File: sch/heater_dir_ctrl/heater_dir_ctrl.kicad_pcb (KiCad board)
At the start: 2 copper layers, 75 parts, among them J1 UV light, J10 main, J11 flashlight, J2 SWD, J3 heater, J4 heater, J5 motor, J6 motor, J7 ac_in, J8 ac_in, J9 ., Q1 MMBTA42, Q2 MMBTA42, Q3 MMBTA42, Q4 MMBTA42, Q5 AO3400, Q6 Q_Photo_NPN_CE, Q7 AO3400, SW1 SW_Push, SW2 SW_Push, U1 XC6206-33, U2 STM32F031F4Px, U4 4069, U5 TM1637, U7 LTV-817, U8 LNK306D

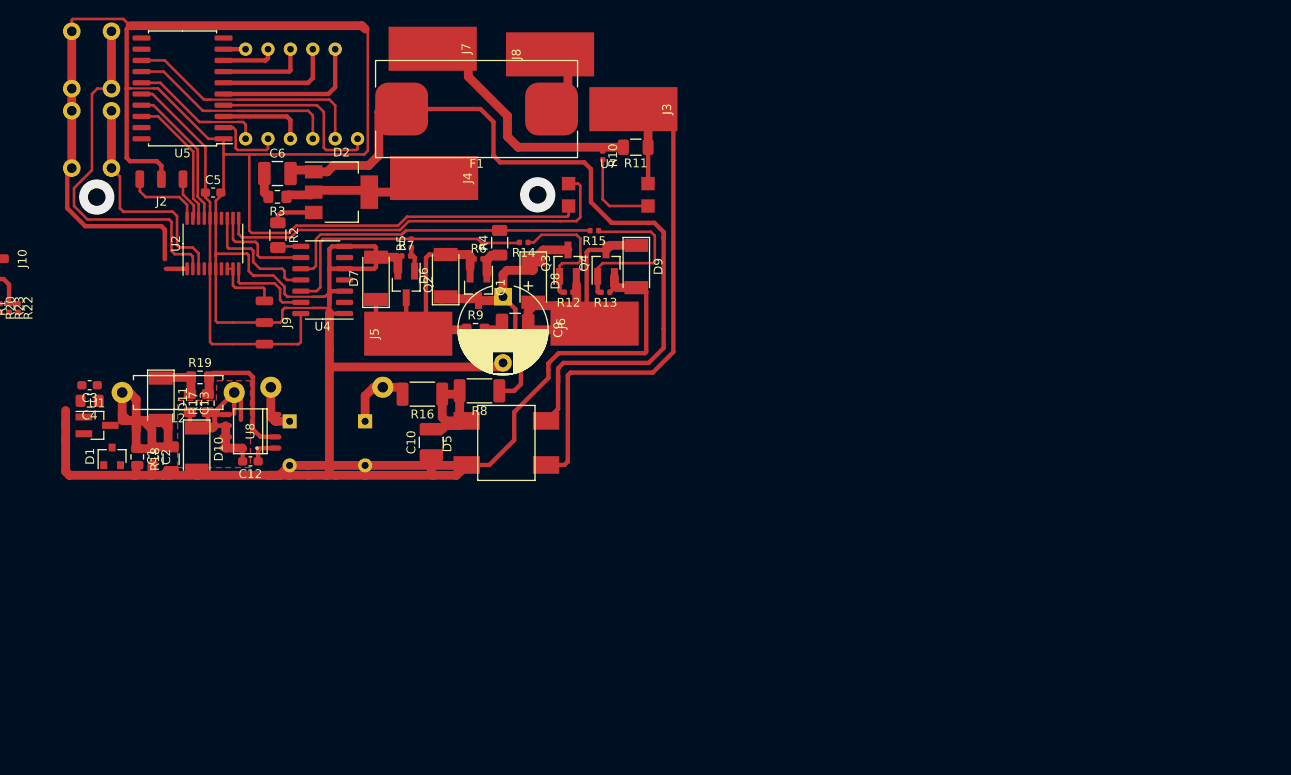
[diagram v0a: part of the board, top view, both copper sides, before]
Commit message: sch w new transistors
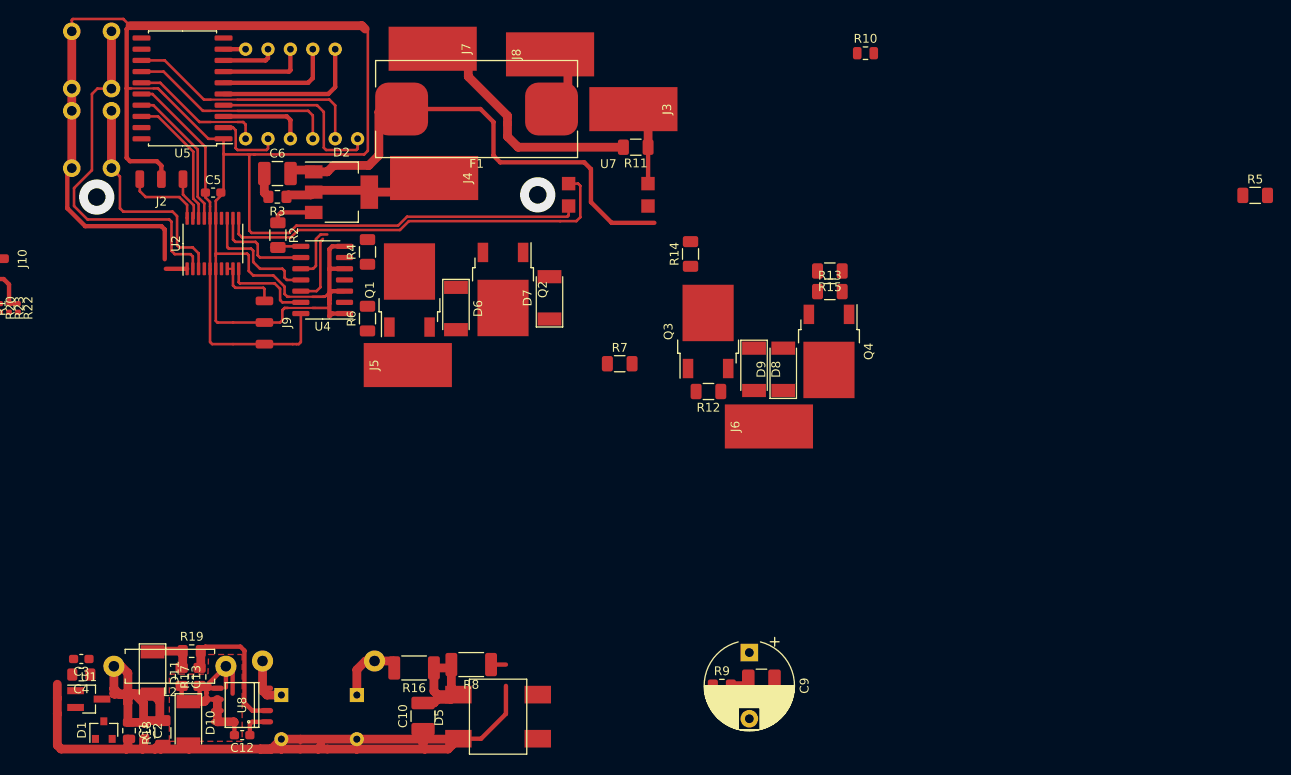
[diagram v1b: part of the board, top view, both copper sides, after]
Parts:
- Q1, Q2, Q3, Q4: value MMBTA42 -> 2N60; footprint Package_TO_SOT_SMD:SOT-23_Handsoldering -> Package_TO_SOT_SMD:TO-252-2
- R10: footprint Resistor_SMD:R_0402_1005Metric -> Resistor_SMD:R_0805_2012Metric
- R12, R13, R14, R15, R5, R6, R7: footprint Resistor_SMD:R_0402_1005Metric -> Resistor_SMD:R_1206_3216Metric
- U2: value STM32F031F4Px -> STM32F031F4P6
- moved R5 95.8 mm to (177.6, 107.0), turned to 0 degrees
- moved C8 49.1 mm to (121.6, 162.1)
- moved C9 49.1 mm to (120.3, 158.8)
- moved R9 49.1 mm to (117.1, 162.6)
- moved R10 32.0 mm to (133.4, 90.9), turned to 0 degrees
- moved C1 31.1 mm to (49.9, 167.7)
- moved C10 31.1 mm to (83.3, 166.0)
- moved C12 31.1 mm to (62.8, 168.2)
- moved C2 31.1 mm to (51.8, 167.7)
- moved C3 31.1 mm to (44.5, 159.6)
- moved C4 31.1 mm to (44.5, 161.3)
- moved L1 31.1 mm to (77.8, 159.8)
- moved R16 31.1 mm to (82.2, 160.6)
- moved R8 31.1 mm to (88.7, 160.2)
- moved U8 31.1 mm to (62.7, 164.8)
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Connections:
- Q1 pad 2: Net-(D6-Pad2) -> Net-(C9-Pad1)
- Q1 pad 3: Net-(C9-Pad1) -> Net-(D6-Pad2)
- Q2 pad 2: GND -> Net-(D6-Pad2)
- Q2 pad 3: Net-(D6-Pad2) -> GND
- Q3 pad 2: Net-(C8-Pad1) -> Net-(C9-Pad1)
- Q3 pad 3: Net-(C9-Pad1) -> Net-(C8-Pad1)
- Q4 pad 2: GND -> Net-(C8-Pad1)
- Q4 pad 3: Net-(C8-Pad1) -> GND
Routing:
- net GND: track 453.4 -> 362.9 mm
- net Net-(D6-Pad2): track 54.7 -> 0.00 mm
- net LINE: track 73.2 -> 21.2 mm
- net Net-(C8-Pad1): track 51.6 -> 0.00 mm
- net NEUT: track 97.4 -> 62.7 mm
- net Net-(C9-Pad1): track 35.2 -> 3.16 mm
- net Net-(R15-Pad2): track 36.6 -> 6.40 mm
- net Net-(R14-Pad2): track 30.6 -> 8.01 mm
- net Net-(Q4-Pad1): track 19.4 -> 0.00 mm
- net Net-(Q3-Pad1): track 15.0 -> 0.00 mm
- net Net-(R10-Pad2): track 9.94 -> 0.00 mm
- net Net-(Q2-Pad1): track 3.38 -> 0.00 mm
- net Net-(Q1-Pad1): track 3.28 -> 0.00 mm

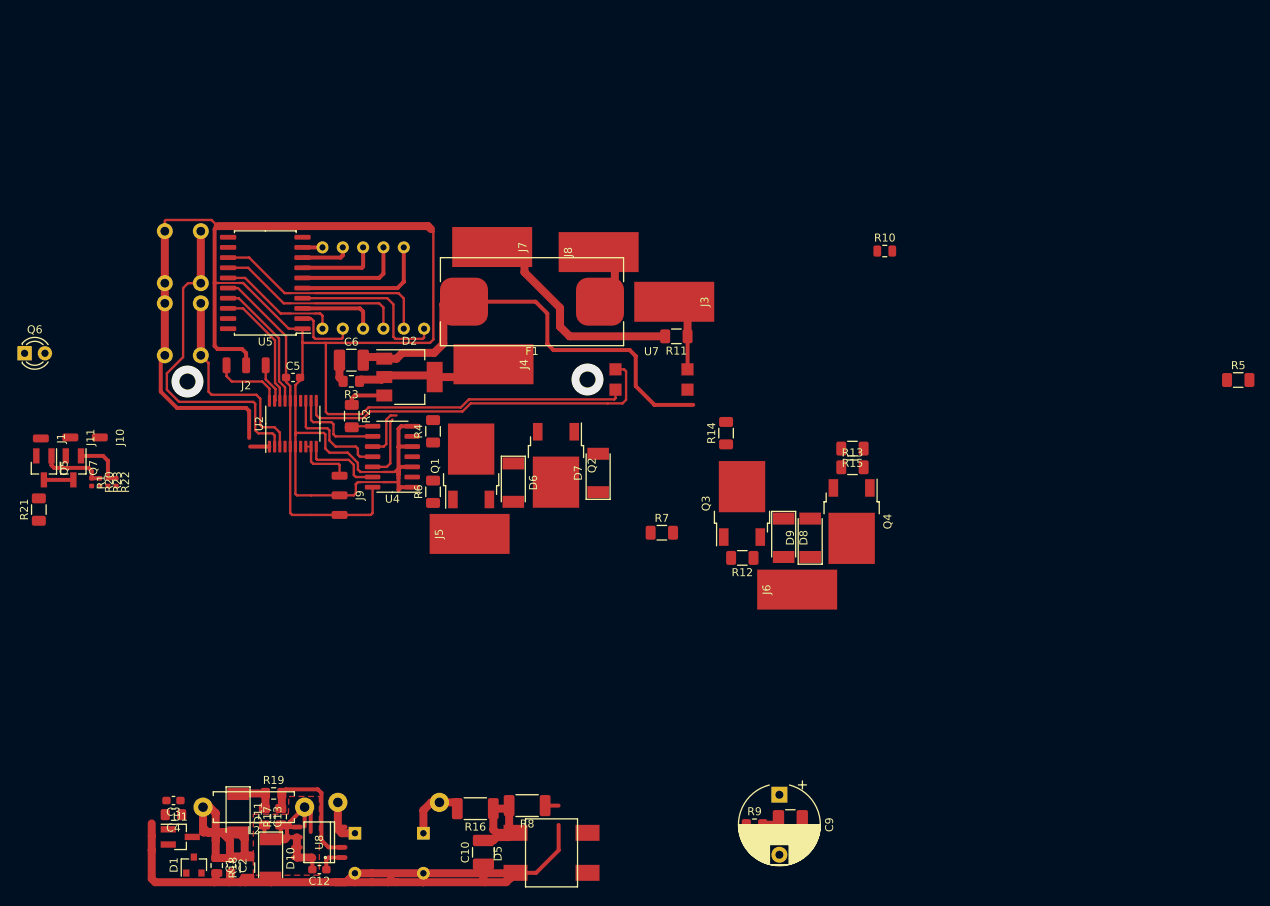
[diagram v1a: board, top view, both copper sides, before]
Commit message: PCB with new transistors
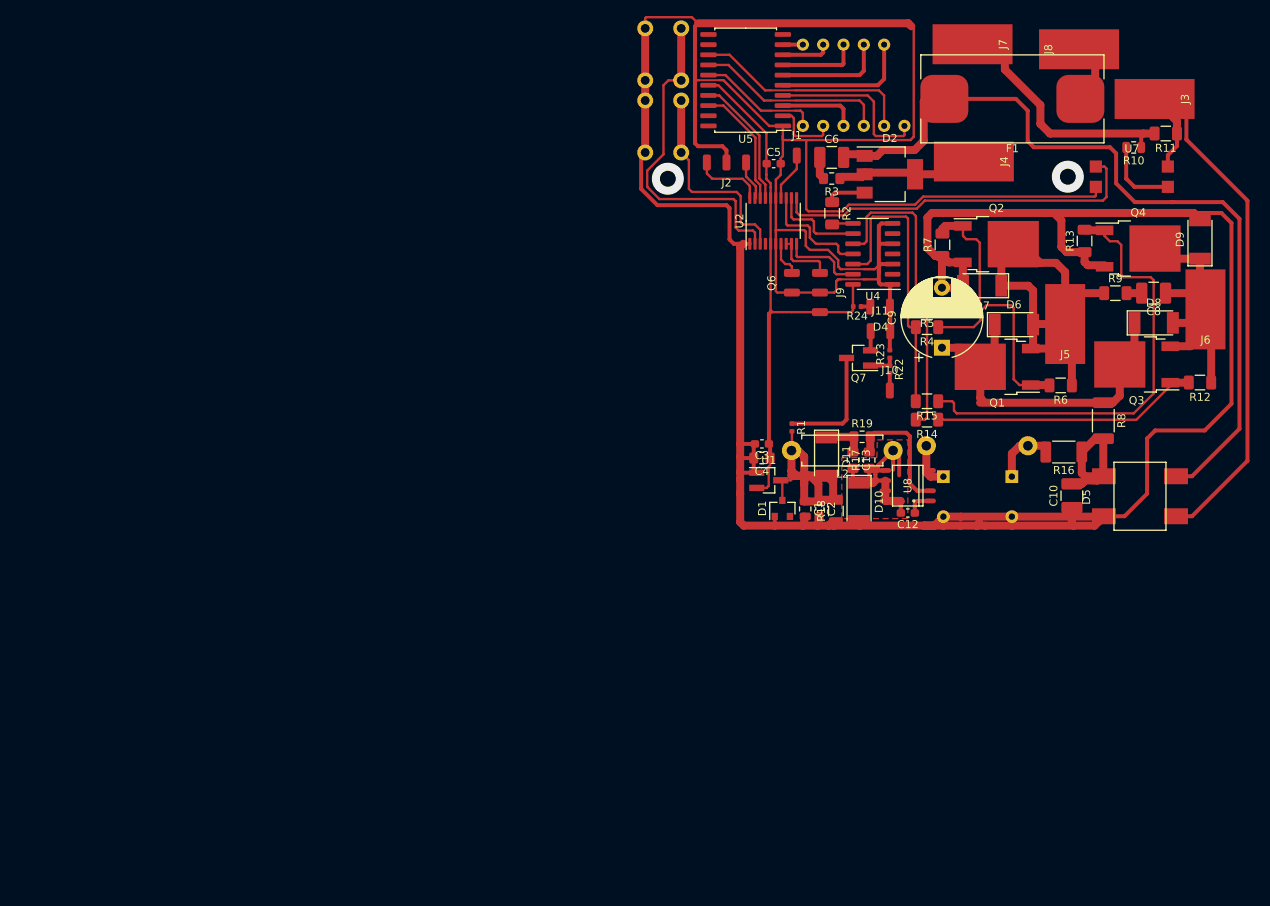
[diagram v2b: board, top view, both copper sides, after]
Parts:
- removed Q5: AO3400, Package_TO_SOT_SMD:SOT-23_Handsoldering
- removed R20: 50, Resistor_SMD:R_0402_1005Metric
- removed R21: 390, Resistor_SMD:R_1206_3216Metric
- added D4: IR204A, local:2WIRE_PADS, F.Cu at (132.9, 97.8)
- added R24: 1k, Resistor_SMD:R_0402_1005Metric, F.Cu at (130.0, 97.8)
- J1: value UV light -> JMP1
- J10: value main -> JMP1
- J11: value flashlight -> UV; footprint Connector_Wire:SolderWirePad_1x01_SMD_1x2mm -> local:2WIRE_PADS
- Q6: footprint LED_THT:LED_D3.0mm -> local:2WIRE_PADS
- R1: value 50 -> 220
- R9: footprint Resistor_SMD:R_0805_2012Metric_Pad1.15x1.40mm_HandSolder -> Resistor_SMD:R_1206_3216Metric
- moved J11 102.1 mm to (132.8, 100.9), turned to 0 degrees
- moved J1 100.9 mm to (122.4, 78.9), turned to 0 degrees
- moved Q7 99.1 mm to (130.1, 104.2), turned to 180 degrees
- moved R23 99.0 mm to (134.1, 103.7), turned to 90 degrees
- moved J10 98.9 mm to (134.1, 108.3), turned to 0 degrees
- moved R22 97.7 mm to (134.1, 105.7)
- moved Q6 96.3 mm to (121.8, 94.9), turned to 90 degrees
- moved R1 87.8 mm to (121.8, 112.9)
- moved R8 86.6 mm to (160.7, 112.1), turned to 270 degrees
- moved C1 86.0 mm to (123.5, 123.1)
- moved C10 86.0 mm to (156.8, 121.5)
- moved C12 86.0 mm to (136.3, 123.6)
- moved C13 86.0 mm to (129.5, 117.0)
- moved C2 86.0 mm to (125.3, 123.1)
- moved C3 86.0 mm to (118.1, 115.0)
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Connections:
- C1 pad 2: Net-(C1-Pad2) -> GND
- C11 pad 2: Net-(C1-Pad2) -> GND
- C2 pad 2: Net-(C1-Pad2) -> GND
- C3 pad 2: Net-(C1-Pad2) -> GND
- C4 pad 2: Net-(C1-Pad2) -> GND
- C7 pad 2: Net-(C1-Pad2) -> GND
- D1 pad 2: Net-(C1-Pad2) -> GND
- D10 pad 2: Net-(C1-Pad2) -> GND
- D5 pad 2: Net-(C1-Pad2) -> GND
- J10 pad 1: GND -> Net-(J10-Pad1)
- Q6 pad 1: Net-(Q6-Pad1) -> GND
- Q6 pad 2: GND -> Net-(Q6-Pad2)
- Q7 pad 3: Net-(Q5-Pad3) -> Net-(Q7-Pad3)
- R1 pad 1: Net-(Q5-Pad1) -> Net-(Q7-Pad3)
- R1 pad 2: Net-(R1-Pad2) -> +5V
- R18 pad 1: Net-(C1-Pad2) -> GND
- R22 pad 2: Net-(R22-Pad2) -> Net-(J10-Pad1)
- U1 pad 1: Net-(C1-Pad2) -> GND
- U2 pad 14: Net-(R1-Pad2) -> Net-(J1-Pad1)
- U2 pad 6: Net-(U2-Pad6) -> GND
- U2 pad 7: Net-(Q6-Pad1) -> Net-(Q6-Pad2)
- U4 pad 1: Net-(R1-Pad2) -> GND
- U4 pad 10: Net-(R15-Pad2) -> Net-(R14-Pad2)
- U4 pad 12: Net-(R14-Pad2) -> Net-(R15-Pad2)
- U4 pad 2: Net-(R22-Pad2) -> Net-(U4-Pad2)
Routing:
- net GND: track 362.9 -> 522.1 mm
- net LINE: track 21.2 -> 87.9 mm
- net Net-(D6-Pad2): track 0.00 -> 60.3 mm
- net Net-(Q4-Pad1): track 0.00 -> 57.4 mm
- net Net-(C8-Pad1): track 0.00 -> 46.7 mm
- net NEUT: track 62.7 -> 108.7 mm
- net Net-(C9-Pad1): track 3.16 -> 44.1 mm
- net Net-(Q3-Pad1): track 0.00 -> 33.5 mm
- net Net-(R14-Pad2): track 8.01 -> 39.4 mm
- net Net-(R15-Pad2): track 6.40 -> 36.2 mm
- net Net-(Q1-Pad1): track 0.00 -> 25.1 mm
- net +3V3: track 46.0 -> 69.7 mm
- net Net-(Q2-Pad1): track 0.00 -> 19.9 mm
- net Net-(Q7-Pad3): track 0.00 -> 14.7 mm
- net Net-(R10-Pad2): track 0.00 -> 9.53 mm
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
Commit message: didn't fit
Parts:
- moved R15 2.17 mm to (136.8, 108.7)
- moved R24 2.16 mm to (127.8, 97.8)
- moved R14 2.16 mm to (136.7, 111.1)
- moved J11 2.03 mm to (130.8, 100.9)
- moved Q7 2.03 mm to (128.1, 104.2)
- moved R22 1.98 mm to (132.1, 105.7)
- moved R23 1.98 mm to (132.1, 103.7)
- moved C8 1.98 mm to (165.1, 96.1)
- moved C9 1.98 mm to (138.6, 103.0)
- moved D4 1.98 mm to (130.9, 97.8)
- moved D6 1.98 mm to (147.6, 100.1)
- moved D7 1.98 mm to (143.6, 95.2)
- moved D8 1.98 mm to (165.1, 99.9)
- moved D9 1.98 mm to (170.8, 89.4)
- moved J10 1.98 mm to (132.1, 108.3)
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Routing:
- net GND: track 522.1 -> 545.3 mm
- net NEUT: track 108.7 -> 118.1 mm
- net +5V: track 41.4 -> 50.3 mm
- net LINE: track 87.9 -> 80.2 mm
- net Net-(SW1-Pad2): track 41.7 -> 38.2 mm
- net VPP: track 18.3 -> 21.5 mm
- net Net-(SW2-Pad2): track 26.2 -> 23.1 mm
- net Net-(U2-Pad11): track 46.6 -> 49.3 mm
- net Net-(J7-Pad1): track 33.4 -> 36.0 mm
- net Net-(Q3-Pad1): track 33.5 -> 35.7 mm
- net Net-(Q7-Pad3): track 14.7 -> 12.7 mm
- net Net-(J1-Pad1): track 6.12 -> 8.09 mm
- net Net-(Q4-Pad1): track 57.4 -> 59.3 mm
- net Net-(D2-Pad3): track 5.03 -> 6.59 mm
- net +3V3: track 69.7 -> 70.9 mm
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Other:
- net class Default: clearance 0.2 -> 0.5
- rule trace_clearance: 0.2 -> 0.5

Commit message: drivers
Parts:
- removed the C8 at (165.1, 96.1)
- removed the C9 at (138.6, 103.0)
- removed the D1 at (120.6, 123.1)
- removed D4: IR204A, local:2WIRE_PADS
- removed the D7 at (143.6, 95.2)
- removed the J10 at (132.1, 108.3)
- removed the J11 at (130.8, 100.9)
- removed the Q3 at (162.9, 105.1)
- removed the R4 at (136.7, 100.4)
- removed the R5 at (136.7, 98.1)
- removed the R6 at (153.4, 107.7)
- removed the R7 at (138.7, 90.1)
- removed the U1 at (118.9, 119.5)
- removed the U4 at (130.3, 91.2)
- added C11: 10uF, Capacitor_SMD:C_0805_2012Metric, F.Cu at (193.0, 94.7)
- added C12: 22uF 400V, Capacitor_THT:CP_Radial_D10.0mm_P7.50mm, F.Cu at (285.9, 51.2)
- added C13: 100n, Capacitor_SMD:C_1210_3225Metric_Pad1.33x2.70mm_HandSolder, F.Cu at (216.7, 94.9)
- added C14: 10uF, Capacitor_SMD:C_0805_2012Metric, F.Cu at (227.9, 100.1)
- added D10: 1N4007, Diode_SMD:D_MELF, F.Cu at (215.4, 100.8)
- added D11: 1N4007, Diode_SMD:D_MELF, F.Cu at (221.1, 84.4)
- added D13: MBR0530, Diode_SMD:D_SOD-123, F.Cu at (232.9, 103.5)
- added D5: MBR0530, Diode_SMD:D_SOD-123, F.Cu at (189.1, 91.3)
- added J2: JMP1, Connector_Wire:SolderWirePad_1x01_SMD_1x2mm, F.Cu at (80.9, 102.7)
- added J3: UV, local:2WIRE_PADS, F.Cu at (79.9, 97.9)
- added Q5: 2N60, Package_TO_SOT_SMD:TO-252-2, F.Cu at (202.1, 100.1)
- added Q6: 2N60, Package_TO_SOT_SMD:TO-252-2, F.Cu at (220.6, 102.2)
- added Q8: DTD114E, Package_TO_SOT_SMD:SOT-23_Handsoldering, F.Cu at (126.9, 86.4)
- added Q9: DTD114E, Package_TO_SOT_SMD:SOT-23_Handsoldering, F.Cu at (233.9, 93.9)
- added R16: 100k, Resistor_SMD:R_0402_1005Metric, F.Cu at (122.4, 83.6)
- added R17: 220, Resistor_SMD:R_1206_3216Metric, F.Cu at (221.5, 95.4)
- added R18: 220, Resistor_SMD:R_1206_3216Metric, F.Cu at (225.7, 88.6)
- added R19: 100k, Resistor_SMD:R_0402_1005Metric, F.Cu at (123.4, 83.6)
- added R20: 220, Resistor_SMD:R_1206_3216Metric, F.Cu at (225.3, 98.6)
- added R21: 220, Resistor_SMD:R_1206_3216Metric, F.Cu at (226.8, 92.0)
- added R25: 100k, Resistor_SMD:R_0402_1005Metric, F.Cu at (231.6, 95.6)
- added R26: 1, Resistor_SMD:R_2010_5025Metric, F.Cu at (191.4, 84.5)
- added R27: 1, Resistor_SMD:R_2010_5025Metric, F.Cu at (215.4, 109.2)
- added R28: 220, Resistor_SMD:R_1206_3216Metric, F.Cu at (182.7, 91.3)
- added R29: 220, Resistor_SMD:R_1206_3216Metric, F.Cu at (182.9, 102.4)
- added U3: AP1117-33, Package_TO_SOT_SMD:SOT-223-3_TabPin2, F.Cu at (117.4, 141.7)
- added U5: IRS2103, Package_SO:SSOP-8_3.9x5.05mm_P1.27mm, F.Cu at (188.2, 95.4)
- added U8: IRS2103, Package_SO:SSOP-8_3.9x5.05mm_P1.27mm, F.Cu at (232.8, 99.4)
- D6: value 1N4007 -> IR204A; footprint Diode_SMD:D_MELF -> local:2WIRE_PADS
- Q1: value 2N60 -> AO3400; footprint Package_TO_SOT_SMD:TO-252-2 -> Package_TO_SOT_SMD:SOT-23_Handsoldering
- Q2: value 2N60 -> DTD114E; footprint Package_TO_SOT_SMD:TO-252-2 -> Package_TO_SOT_SMD:SOT-23_Handsoldering
- Q7: value AO3400 -> 2N60; footprint Package_TO_SOT_SMD:SOT-23_Handsoldering -> Package_TO_SOT_SMD:TO-252-2
- R10: value 1к -> 100; footprint Resistor_SMD:R_0805_2012Metric -> Resistor_SMD:R_2010_5025Metric
- R11: value 1 -> 220
- R2: value 220 -> 50; footprint Resistor_SMD:R_1206_3216Metric -> Resistor_SMD:R_0402_1005Metric
- R22: value 50 -> 1к
- R23: value 50 -> 1; footprint Resistor_SMD:R_0402_1005Metric -> Resistor_SMD:R_2010_5025Metric
- R24: footprint Resistor_SMD:R_0402_1005Metric -> Resistor_SMD:R_1206_3216Metric
- R3: value 1k -> 50; footprint Resistor_SMD:R_0805_2012Metric_Pad1.15x1.40mm_HandSolder -> Resistor_SMD:R_0402_1005Metric
- R8: value 100 -> 100k; footprint Resistor_SMD:R_2010_5025Metric -> Resistor_SMD:R_0402_1005Metric
- R9: value 220 -> 1k; footprint Resistor_SMD:R_1206_3216Metric -> Resistor_SMD:R_0402_1005Metric
- moved Q7 92.0 mm to (219.0, 89.6)
- moved R15 75.6 mm to (211.1, 95.2), turned to 0 degrees
- moved Q1 70.4 mm to (75.2, 102.1)
- moved D6 64.5 mm to (205.7, 128.0)
- moved R14 59.4 mm to (195.4, 101.6), turned to 270 degrees
- moved R10 59.4 mm to (207.5, 120.1), turned to 270 degrees
- moved J5 56.5 mm to (210.5, 102.2)
- moved R9 55.3 mm to (207.0, 125.7), turned to 90 degrees
- moved R3 53.3 mm to (78.4, 104.0), turned to 270 degrees
- moved R13 49.2 mm to (205.3, 95.2), turned to 0 degrees
- moved R2 49.1 mm to (78.9, 102.6), turned to 0 degrees
- moved R23 45.7 mm to (168.9, 76.7), turned to 180 degrees
- moved R22 43.1 mm to (164.6, 77.5)
- moved Q2 43.0 mm to (187.0, 100.9), turned to 90 degrees
- moved J6 40.2 mm to (210.5, 88.2)
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- renumbered C5 to C1, C4 to C10, C6 to C15, C10 to C2, C7 to C3, C11 to C4, C12 to C5, C13 to C6, C1 to C7, C2 to C8, C3 to C9, D5 to D1, D2 to D12, D10 to D2, D11 to D3, D3 to D7, J3 to J10, J4 to J11, J2 to J4, J9 to J7, J7 to J8, J8 to J9, Q6 to Q3, R16 to R1, R17 to R4, R1 to R5, R19 to R6, R18 to R7, U2 to U1, U8 to U2, U5 to U4, U7 to U6
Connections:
- C15 pad 1: Net-(C6-Pad1) (its old number) -> Net-(C15-Pad1)
- C7 pad 1: +5V -> +10V
- C8 pad 1: +5V -> +10V
- D12 pad 2: Net-(D2-Pad2) -> Net-(D12-Pad2)
- D12 pad 3: Net-(D2-Pad3) -> Net-(D12-Pad3)
- D12 pad 4: Net-(D2-Pad2) -> Net-(D12-Pad2)
- D3 pad 2: +5V -> +10V
- D6 pad 1: Net-(C9-Pad1) -> GND
- D8 pad 1: Net-(C9-Pad1) -> Net-(D8-Pad1)
- D8 pad 2: Net-(C8-Pad1) -> Net-(C11-Pad2)
- D9 pad 1: Net-(C8-Pad1) -> Net-(C11-Pad2)
- J11 pad 1: Net-(D2-Pad2) -> Net-(D12-Pad2)
- J5 pad 1: Net-(D6-Pad2) -> Net-(C11-Pad2)
- J6 pad 1: Net-(C8-Pad1) -> Net-(C13-Pad1)
- J8 pad 1: Net-(J7-Pad1) -> Net-(J8-Pad1)
- L2 pad 2: +5V -> +10V
- Q1 pad 2: Net-(C9-Pad1) -> Net-(J3-Pad1)
- Q1 pad 3: Net-(D6-Pad2) -> Net-(Q1-Pad3)
- Q2 pad 2: Net-(D6-Pad2) -> GND
- Q2 pad 3: GND -> Net-(Q2-Pad3)
- Q3 pad 2: Net-(Q6-Pad2) -> Net-(Q3-Pad2)
- Q4 pad 2: Net-(C8-Pad1) -> Net-(D8-Pad1)
- Q4 pad 3: GND -> Net-(C11-Pad2)
- Q7 pad 2: Net-(J11-Pad1) -> Net-(C13-Pad1)
- Q7 pad 3: Net-(Q7-Pad3) -> GND
- R10 pad 1: Net-(J7-Pad1) -> Net-(C12-Pad1)
- R10 pad 2: Net-(R10-Pad2) -> VPP
- R11 pad 1: LINE -> Net-(Q4-Pad1)
- R11 pad 2: Net-(J7-Pad1) -> Net-(R11-Pad2)
- R12 pad 1: Net-(C8-Pad1) -> Net-(Q5-Pad1)
- R12 pad 2: Net-(Q3-Pad1) -> Net-(R12-Pad2)
- R13 pad 1: GND -> Net-(Q4-Pad1)
- R13 pad 2: Net-(Q4-Pad1) -> Net-(C11-Pad2)
- R14 pad 1: Net-(Q3-Pad1) -> Net-(Q5-Pad1)
- R14 pad 2: Net-(R14-Pad2) -> GND
- R15 pad 1: Net-(Q4-Pad1) -> Net-(C11-Pad2)
- R2 pad 1: Net-(D2-Pad3) -> Net-(Q1-Pad1)
- R22 pad 1: Net-(Q7-Pad1) -> Net-(J8-Pad1)
- R22 pad 2: Net-(J10-Pad1) -> Net-(R22-Pad2)
- R23 pad 1: Net-(Q7-Pad1) -> LINE
- R23 pad 2: GND -> Net-(J8-Pad1)
- R24 pad 1: Net-(D4-Pad2) -> Net-(D12-Pad2)
- R24 pad 2: +3V3 -> Net-(C15-Pad1)
- R3 pad 1: Net-(D2-Pad2) -> Net-(Q1-Pad1)
- R3 pad 2: Net-(C6-Pad1) (its old number) -> GND
- R5 pad 1: Net-(Q7-Pad3) -> Net-(Q1-Pad3)
- R5 pad 2: +5V -> +10V
- R7 pad 2: +5V -> +10V
- R8 pad 1: Net-(C9-Pad1) -> Net-(Q2-Pad1)
- R8 pad 2: VPP -> +10V
- R9 pad 2: Net-(C8-Pad2) -> +3V3
- U1 pad 11: Net-(U2-Pad11) -> Net-(U1-Pad11)
- U1 pad 7: Net-(Q6-Pad2) -> Net-(U1-Pad7)
- U6 pad 1: Net-(R10-Pad2) -> Net-(R22-Pad2)
- U6 pad 4: Net-(U2-Pad11) -> Net-(U6-Pad4)
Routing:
- net GND: track 545.3 -> 387.5 mm
- net +10V: track 0.00 -> 63.3 mm
- net LINE: track 80.2 -> 18.3 mm
- net Net-(D6-Pad2): track 60.3 -> 0.00 mm
- net Net-(C11-Pad2): track 0.00 -> 53.8 mm
- net NEUT: track 118.1 -> 66.7 mm
- net +5V: track 50.3 -> 0.00 mm
- net Net-(Q4-Pad1): track 59.3 -> 9.19 mm
- net Net-(U2-Pad11): track 49.3 -> 0.00 mm
- net Net-(C8-Pad1): track 46.7 -> 0.00 mm
- net Net-(C9-Pad1): track 44.7 -> 0.00 mm
- net Net-(C13-Pad1): track 0.00 -> 42.2 mm
- net Net-(R14-Pad2): track 39.0 -> 0.00 mm
- net Net-(J7-Pad1): track 36.0 -> 0.00 mm
- net Net-(Q3-Pad1): track 35.7 -> 0.00 mm
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
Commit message: commas
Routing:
- net Net-(Q6-Pad1): track 2.56 -> 5.32 mm
